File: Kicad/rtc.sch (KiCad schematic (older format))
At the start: 6 parts, among them U901 MCP7940, Y901 32,768 Hz

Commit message: Switching some parts over to the CPL.
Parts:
- C903: Digikey BC1150CT-ND -> (none); MPN K104K15X7RF5TL2 -> CPL-CAP-X7R-0805-100NF-50V; Manufacturer Vishay -> CPL; Mouser 594-K104K15X7RF5TL2 -> (none)
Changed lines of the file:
@@
 $Descr A4 11693 8268
 encoding utf-8
-Sheet 11 11
+Sheet 9 11
 Title "Neotron Common Hardware - Real Time Clock"
 Date "2021-04-17"
@@
 F 2 "Capacitor_SMD:C_0805_2012Metric_Pad1.18x1.45mm_HandSolder" H 7088 3200 50  0001 C CNN
 F 3 "~" H 7050 3350 50  0001 C CNN
-F 4 "Vishay" H 0   0   50  0001 C CNN "Manufacturer"
+F 4 "CPL" H 0   0   50  0001 C CNN "Manufacturer"
 F 5 "0" H 7050 3350 50  0001 C CNN "DNP"
-F 6 "BC1150CT-ND" H 7050 3350 50  0001 C CNN "Digikey"
-F 7 "K104K15X7RF5TL2" H 7050 3350 50  0001 C CNN "MPN"
-F 8 "594-K104K15X7RF5TL2" H 7050 3350 50  0001 C CNN "Mouser"
+F 6 "" H 7050 3350 50  0001 C CNN "Digikey"
+F 7 "CPL-CAP-X7R-0805-100NF-50V" H 7050 3350 50  0001 C CNN "MPN"
+F 8 "" H 7050 3350 50  0001 C CNN "Mouser"
 	1    7050 3350
 	1    0    0    -1

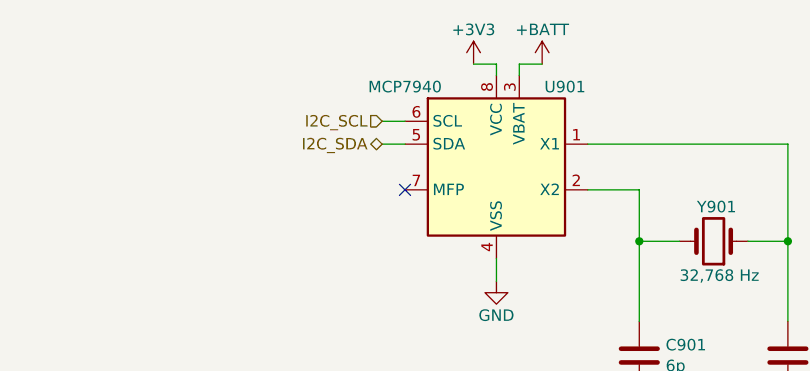
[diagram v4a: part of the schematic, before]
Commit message: Fixing some review comments.
* PCB has rounded corners.
* Add JLCPCB part numbers for SMT parts
* Fixed Fab layer
* Renumbered Slots
* Mounting holes do not have thermal relief

Closes #13 #12 and #10
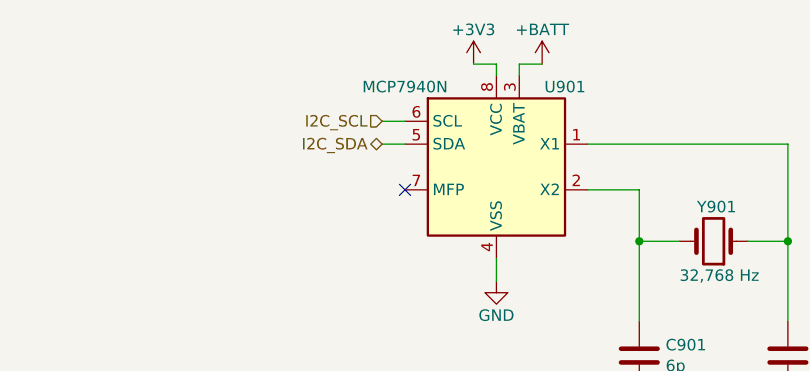
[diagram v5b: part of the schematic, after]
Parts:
- C901, C902: LCSC Part# (none) -> C1828
- C903: LCSC Part# (none) -> C49678
- U901: value MCP7940 -> MCP7940N; LCSC Part# (none) -> C51106
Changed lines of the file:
@@
 P 4075 2675
 F 0 "U901" H 4375 3025 50  0000 C CNN
-F 1 "MCP7940" H 3675 3025 50  0000 C CNN
+F 1 "MCP7940N" H 3675 3025 50  0000 C CNN
 F 2 "Package_SO:SOIC-8_3.9x4.9mm_P1.27mm" H 4075 2675 50  0001 C CNN
 F 3 "http://ww1.microchip.com/downloads/en/DeviceDoc/20005010F.pdf" H 4075 2675 50  0001 C CNN
@@
 F 7 "MCP7940NT-I/SNCT-ND" H 4075 2675 50  0001 C CNN "Digikey"
 F 8 "579-MCP7940NT-I/SN" H 4075 2675 50  0001 C CNN "Mouser"
+F 9 "C51106" H 4075 2675 50  0001 C CNN "LCSC Part#"
 	1    4075 2675
 	1    0    0    -1
@@
 F 6 "103" H 6300 3400 50  0001 C CNN "MPN"
 F 7 "36-103-ND" H 6300 3400 50  0001 C CNN "Digikey"
+F 8 "~" H 6300 3400 50  0001 C CNN "LCSC Part#"
 	1    6300 3400
 	1    0    0    -1
@@
 F 7 "CPL-CAP-X7R-0805-100NF-50V" H 7050 3350 50  0001 C CNN "MPN"
 F 8 "" H 7050 3350 50  0001 C CNN "Mouser"
+F 9 "C49678" H 7050 3350 50  0001 C CNN "LCSC Part#"
 	1    7050 3350
 	1    0    0    -1
@@
 F 7 "300-8301-ND" H 5025 3000 50  0001 C CNN "Digikey"
 F 8 "CFS-20632768DZBB" H 5025 3000 50  0001 C CNN "Mouser"
+F 9 "~" H 5025 3000 50  0001 C CNN "LCSC Part#"
 	1    5025 3000
 	-1   0    0    1
@@
 F 7 "311-1095-1-ND" H 5350 3500 50  0001 C CNN "Digikey"
 F 8 "603-CC805DRNPO9BN6R0" H 5350 3500 50  0001 C CNN "Mouser"
+F 9 "C1828" H 5350 3500 50  0001 C CNN "LCSC Part#"
 	1    5350 3500
 	1    0    0    -1
@@
 F 7 "311-1095-1-ND" H 4700 3500 50  0001 C CNN "Digikey"
 F 8 "603-CC805DRNPO9BN6R0" H 4700 3500 50  0001 C CNN "Mouser"
+F 9 "C1828" H 4700 3500 50  0001 C CNN "LCSC Part#"
 	1    4700 3500
 	1    0    0    -1

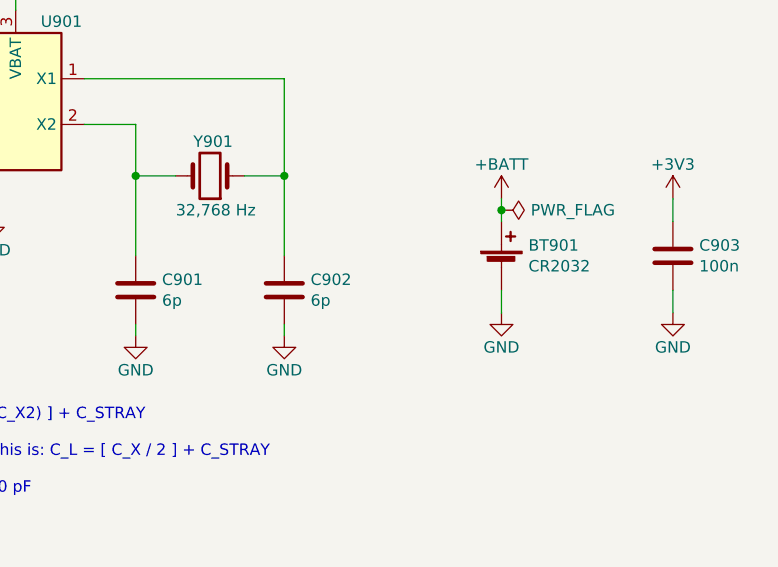
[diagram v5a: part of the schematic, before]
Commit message: BoM and PCB fixes.
* Move tolerances and voltages out of value and into their own fields.
* Fix 5V trace for audio stage.
* Fixup docs.yml so outputs work for JLCPCB.
* Fix JLCPCB part number for 22pF caps.
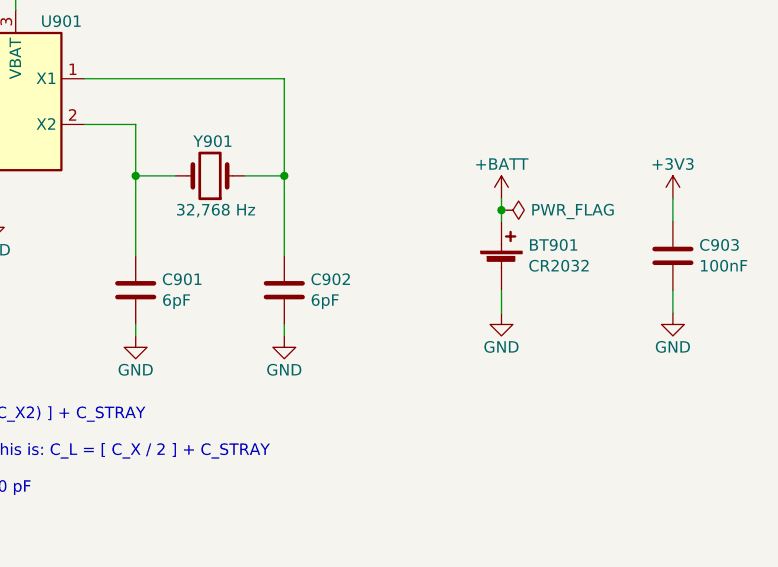
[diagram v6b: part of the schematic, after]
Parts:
- C901, C902: value 6p -> 6pF; Voltage (none) -> C0G
- C903: value 100n -> 100nF
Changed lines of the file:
@@
 AR Path="/5FEF404D/5E0203CB" Ref="C903"  Part="1"
 F 0 "C903" H 7165 3396 50  0000 L CNN
-F 1 "100n" H 7165 3305 50  0000 L CNN
+F 1 "100nF" H 7165 3305 50  0000 L CNN
 F 2 "Capacitor_SMD:C_0805_2012Metric_Pad1.18x1.45mm_HandSolder" H 7088 3200 50  0001 C CNN
 F 3 "~" H 7050 3350 50  0001 C CNN
@@
 P 5350 3500
 F 0 "C902" H 5465 3546 50  0000 L CNN
-F 1 "6p" H 5465 3455 50  0000 L CNN
+F 1 "6pF" H 5465 3455 50  0000 L CNN
 F 2 "Capacitor_SMD:C_0805_2012Metric_Pad1.18x1.45mm_HandSolder" H 5388 3350 50  0001 C CNN
 F 3 "~" H 5350 3500 50  0001 C CNN
@@
 F 8 "603-CC805DRNPO9BN6R0" H 5350 3500 50  0001 C CNN "Mouser"
 F 9 "C1828" H 5350 3500 50  0001 C CNN "LCSC Part#"
+F 10 "C0G" H 5350 3500 50  0001 C CNN "Voltage"
 	1    5350 3500
 	1    0    0    -1
@@
 P 4700 3500
 F 0 "C901" H 4815 3546 50  0000 L CNN
-F 1 "6p" H 4815 3455 50  0000 L CNN
+F 1 "6pF" H 4815 3455 50  0000 L CNN
 F 2 "Capacitor_SMD:C_0805_2012Metric_Pad1.18x1.45mm_HandSolder" H 4738 3350 50  0001 C CNN
 F 3 "~" H 4700 3500 50  0001 C CNN
@@
 F 8 "603-CC805DRNPO9BN6R0" H 4700 3500 50  0001 C CNN "Mouser"
 F 9 "C1828" H 4700 3500 50  0001 C CNN "LCSC Part#"
+F 10 "C0G" H 4700 3500 50  0001 C CNN "Voltage"
 	1    4700 3500
 	1    0    0    -1

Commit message: Feature/swap layers (#22)
* Switch around the layers.

We now have:

1. Signal + Ground
2. Power (3.3V)
3. Ground
4. Signal + Power (3.3V)

This balances things a bit better than Sig/Gnd, Power, Ground, Sig/Gnd.

* Replace MCP7940N with DIP. Also enlarge some caps.

The capacitor footprints were just too small for such large value
electrolytics. The RTC footprint was due to availability.
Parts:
- U901: footprint Package_SO:SOIC-8_3.9x4.9mm_P1.27mm -> Package_DIP:DIP-8_W7.62mm; Digikey MCP7940NT-I/SNCT-ND -> MCP7940N-I/P-ND; MPN MCP7940NT-I/SN -> MCP7940N-I/P; Mouser 579-MCP7940NT-I/SN -> 579-MCP7940N-I/P
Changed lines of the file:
@@
 Sheet 9 11
 Title "Neotron Common Hardware - Real Time Clock"
-Date "2021-06-03"
+Date "2021-06-10"
 Rev "[Uncontrolled]"
 Comp "https://neotron-compute.github.io/"
@@
 F 0 "U901" H 4375 3025 50  0000 C CNN
 F 1 "MCP7940N" H 3675 3025 50  0000 C CNN
-F 2 "Package_SO:SOIC-8_3.9x4.9mm_P1.27mm" H 4075 2675 50  0001 C CNN
+F 2 "Package_DIP:DIP-8_W7.62mm" H 4075 2675 50  0001 C CNN
 F 3 "http://ww1.microchip.com/downloads/en/DeviceDoc/20005010F.pdf" H 4075 2675 50  0001 C CNN
 F 4 "Microchip" H 4075 2675 50  0001 C CNN "Manufacturer"
 F 5 "0" H 4075 2675 50  0001 C CNN "DNP"
-F 6 "MCP7940NT-I/SN" H 4075 2675 50  0001 C CNN "MPN"
-F 7 "MCP7940NT-I/SNCT-ND" H 4075 2675 50  0001 C CNN "Digikey"
-F 8 "579-MCP7940NT-I/SN" H 4075 2675 50  0001 C CNN "Mouser"
+F 6 "MCP7940N-I/P" H 4075 2675 50  0001 C CNN "MPN"
+F 7 "MCP7940N-I/P-ND" H 4075 2675 50  0001 C CNN "Digikey"
+F 8 "579-MCP7940N-I/P" H 4075 2675 50  0001 C CNN "Mouser"
 F 9 "C51106" H 4075 2675 50  0001 C CNN "LCSC Part#"
 	1    4075 2675

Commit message: Fix part nos for C901 and C902.
These were swapped manually when the JLCPCB order was
placed for v0.5.0.
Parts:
- C901, C902: LCSC Part# C1828 -> C67560
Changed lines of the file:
@@
 F 7 "311-1095-1-ND" H 5350 3500 50  0001 C CNN "Digikey"
 F 8 "603-CC805DRNPO9BN6R0" H 5350 3500 50  0001 C CNN "Mouser"
-F 9 "C1828" H 5350 3500 50  0001 C CNN "LCSC Part#"
+F 9 "C67560" H 5350 3500 50  0001 C CNN "LCSC Part#"
 F 10 "C0G" H 5350 3500 50  0001 C CNN "Voltage"
 	1    5350 3500
@@
 F 7 "311-1095-1-ND" H 4700 3500 50  0001 C CNN "Digikey"
 F 8 "603-CC805DRNPO9BN6R0" H 4700 3500 50  0001 C CNN "Mouser"
-F 9 "C1828" H 4700 3500 50  0001 C CNN "LCSC Part#"
+F 9 "C67560" H 4700 3500 50  0001 C CNN "LCSC Part#"
 F 10 "C0G" H 4700 3500 50  0001 C CNN "Voltage"
 	1    4700 3500
